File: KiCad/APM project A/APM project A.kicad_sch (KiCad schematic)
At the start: 18 parts, among them M1 DC_MOTOR, M2 DC_MOTOR, U1 ultrasone_sensor, U2 ultrasone_sensor, U3 L293D

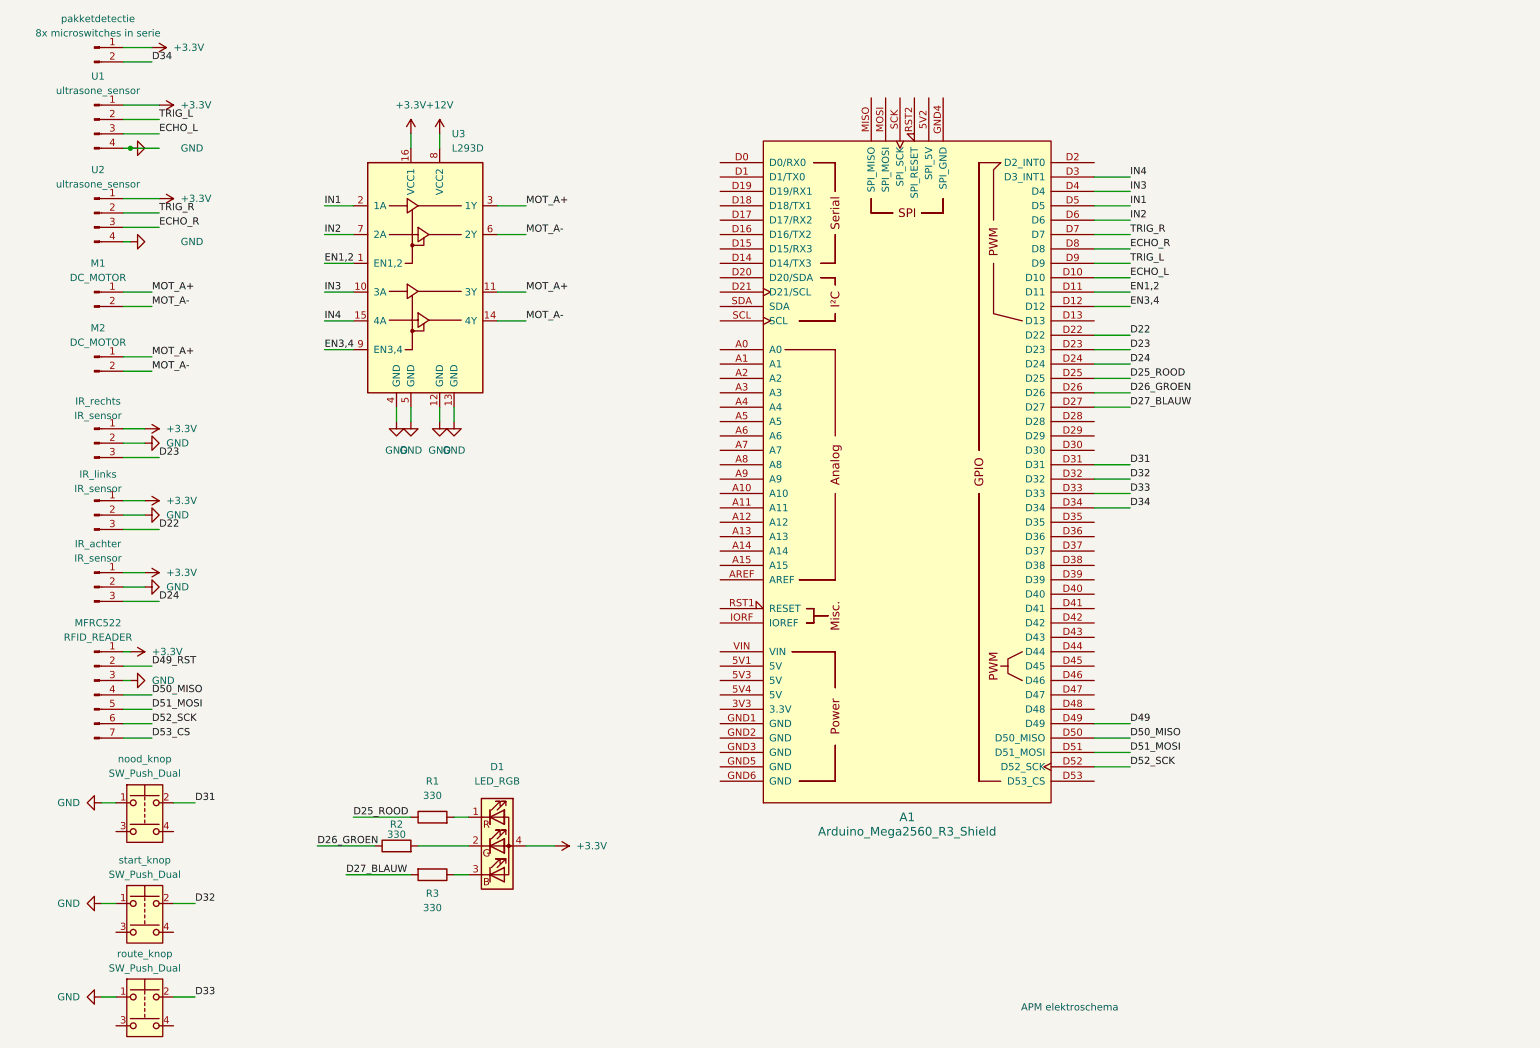
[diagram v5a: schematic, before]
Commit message: IR sensor, ultrasone sensor code werkend. laatste aanpassing elektrisch schema
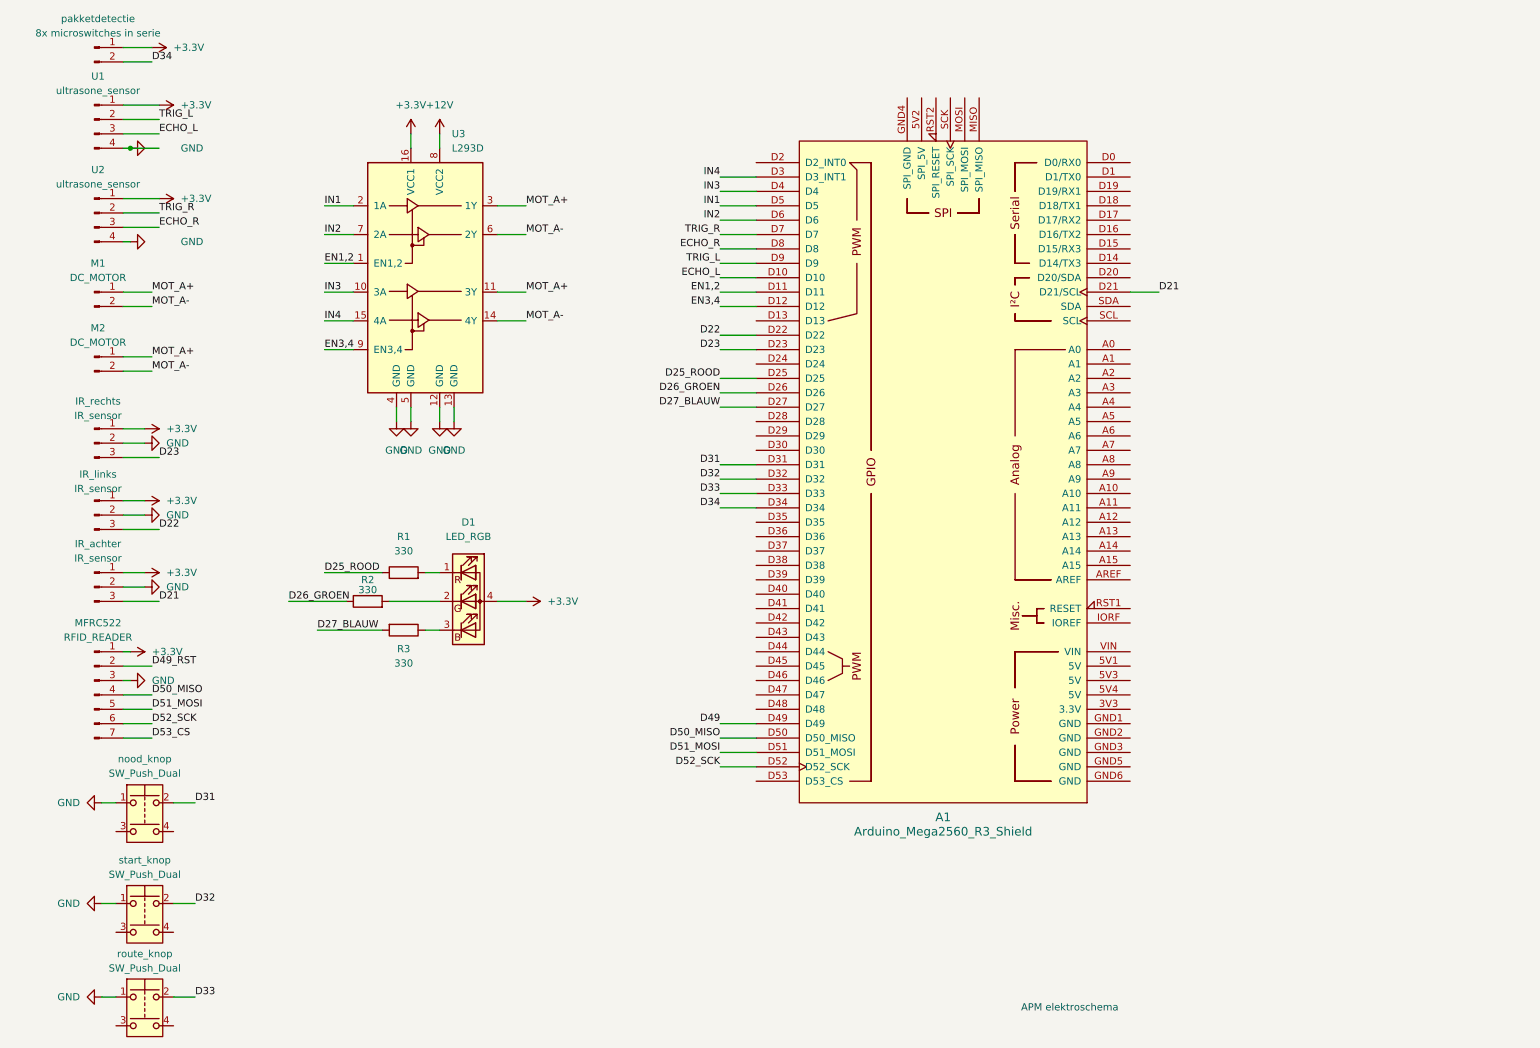
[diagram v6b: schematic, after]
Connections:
- net D21: now reaches A1.D21 (D21/SCL)
- net D21: now also IR_achter.3 (Pin_3)
- net D24: no longer names the net of A1.D24
- net D24: no longer IR_achter.3 (Pin_3)
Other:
- moved on the sheet: A1, D1, R1, R2, R3
